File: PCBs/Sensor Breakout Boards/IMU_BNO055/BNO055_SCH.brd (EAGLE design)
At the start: 25.4 x 25.4 mm, 6 parts

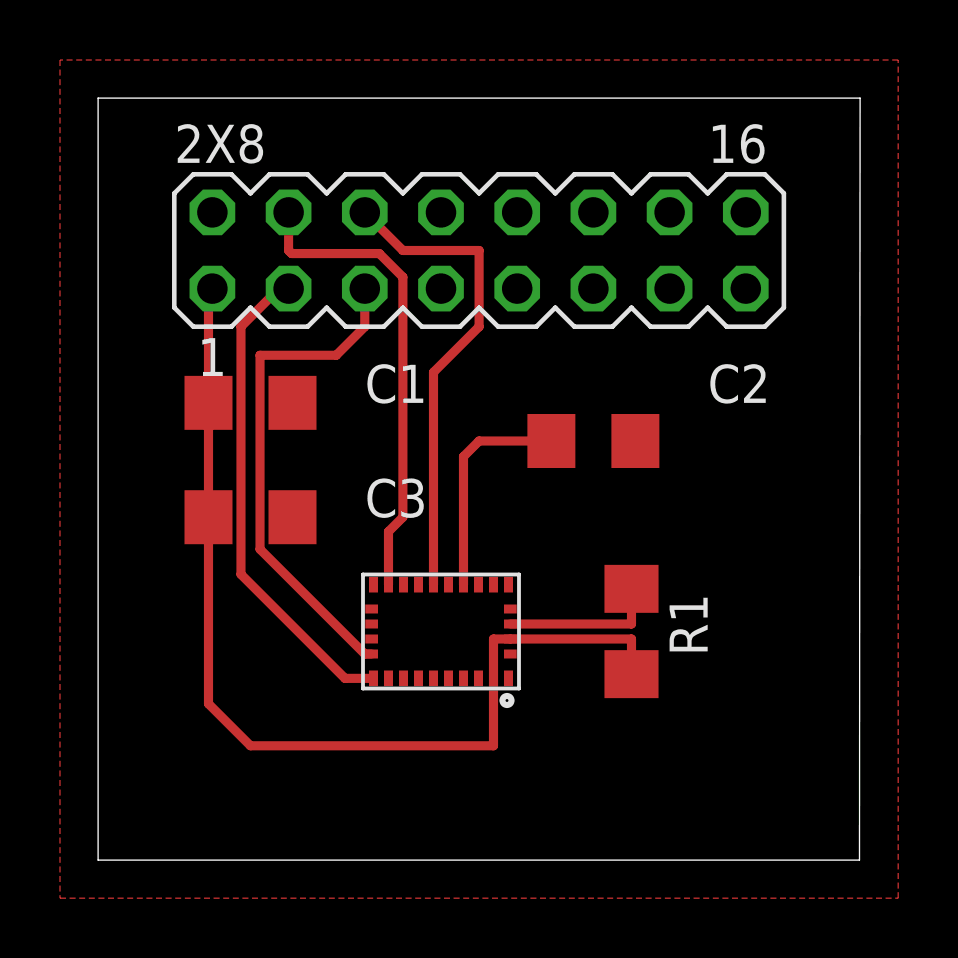
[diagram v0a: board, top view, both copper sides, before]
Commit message: actually updated the imu board, might want to check clearance before shipping it out
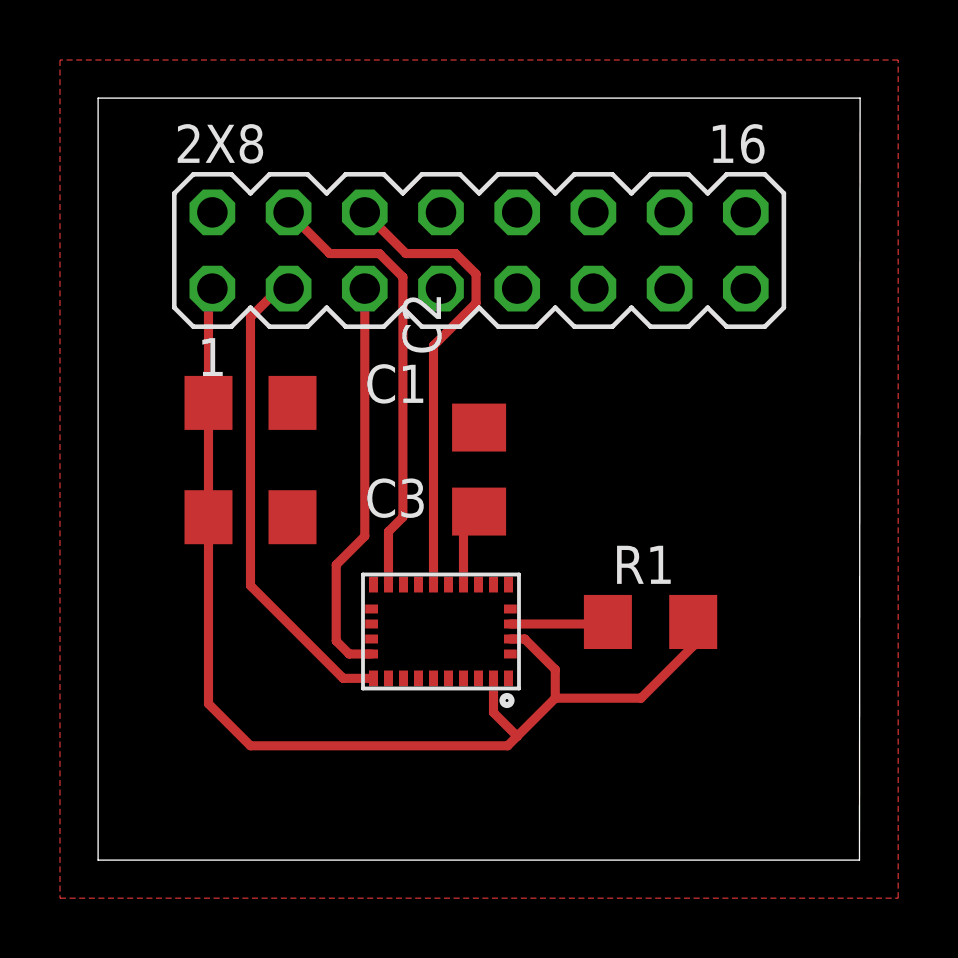
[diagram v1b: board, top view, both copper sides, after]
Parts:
- moved C2 3.93 mm to (12.7, 13.0), turned to 90 degrees
- moved R1 0.71 mm to (18.4, 7.94), turned to 0 degrees
- renumbered BNO055 to U1
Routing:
- net N$3: track 7.41 -> 2.65 mm
- net VCC: track 33.4 -> 37.9 mm
- net SCL: track 16.8 -> 13.5 mm
- net BOOT: track 5.21 -> 3.28 mm
- net INT: track 15.9 -> 15.2 mm
- net RST: track 16.1 -> 15.5 mm
